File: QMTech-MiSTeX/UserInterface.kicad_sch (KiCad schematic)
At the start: 11 parts, among them SW1 XKB5858-W-F-75, SW2 TS-1187A-B-A-B, SW3 TS-1187A-B-A-B, SW4 TS-1187A-B-A-B, SW5 TS-1187A-B-A-B

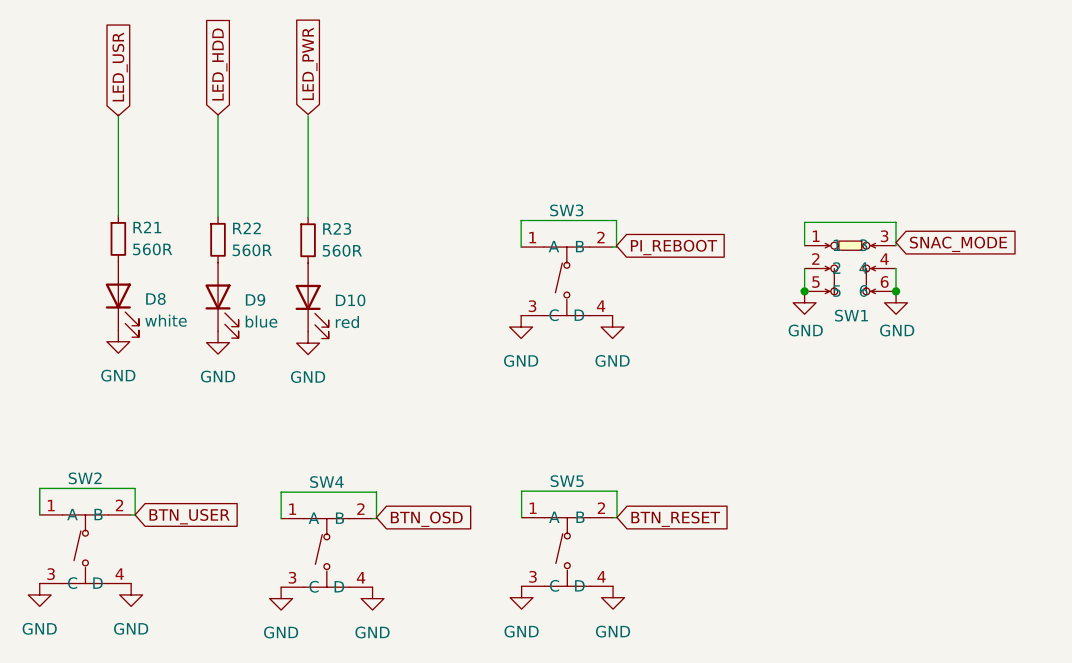
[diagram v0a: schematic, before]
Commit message: apply review notes from somhi, move audio into its own subsheet, add analog audio out
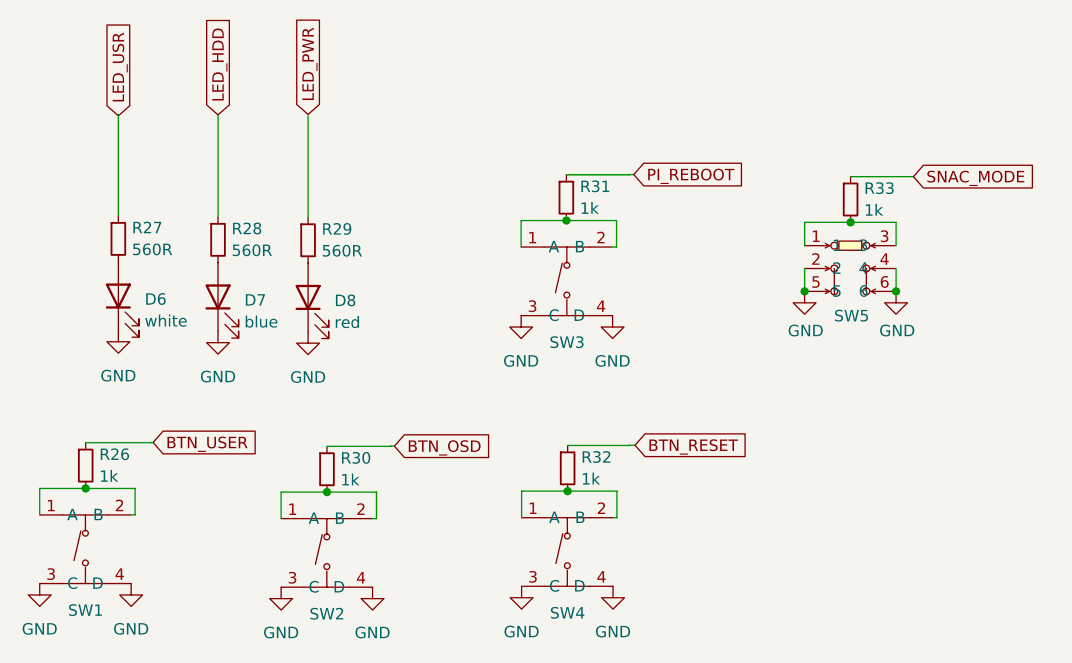
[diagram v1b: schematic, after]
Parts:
- added R26, R30, R31, R32, R33: 1k, R_0402_1005Metric, symbol jlcpcb-basic-resistor-0402:1k
- renumbered D8 to D6, D9 to D7, D10 to D8, R21 to R27, R22 to R28, R23 to R29, SW2 to SW1, SW4 to SW2, SW5 to SW4, SW1 to SW5
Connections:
- net BTN_OSD: now also R30.1; no longer SW2.1 (A), SW2.2 (B)
- net BTN_RESET: now also R32.1; no longer SW4.1 (A), SW4.2 (B)
- net BTN_USER: now also R26.1; no longer SW1.1 (A), SW1.2 (B)
- net PI_REBOOT: now also R31.1; no longer SW3.1 (A), SW3.2 (B)
- net SNAC_MODE: now also R33.1; no longer SW5.1, SW5.3
- new net: R32.2, SW4.1 (A), SW4.2 (B)
- new net: R33.2, SW5.1, SW5.3
- new net: R26.2, SW1.1 (A), SW1.2 (B)
- new net: R31.2, SW3.1 (A), SW3.2 (B)
- new net: R30.2, SW2.1 (A), SW2.2 (B)

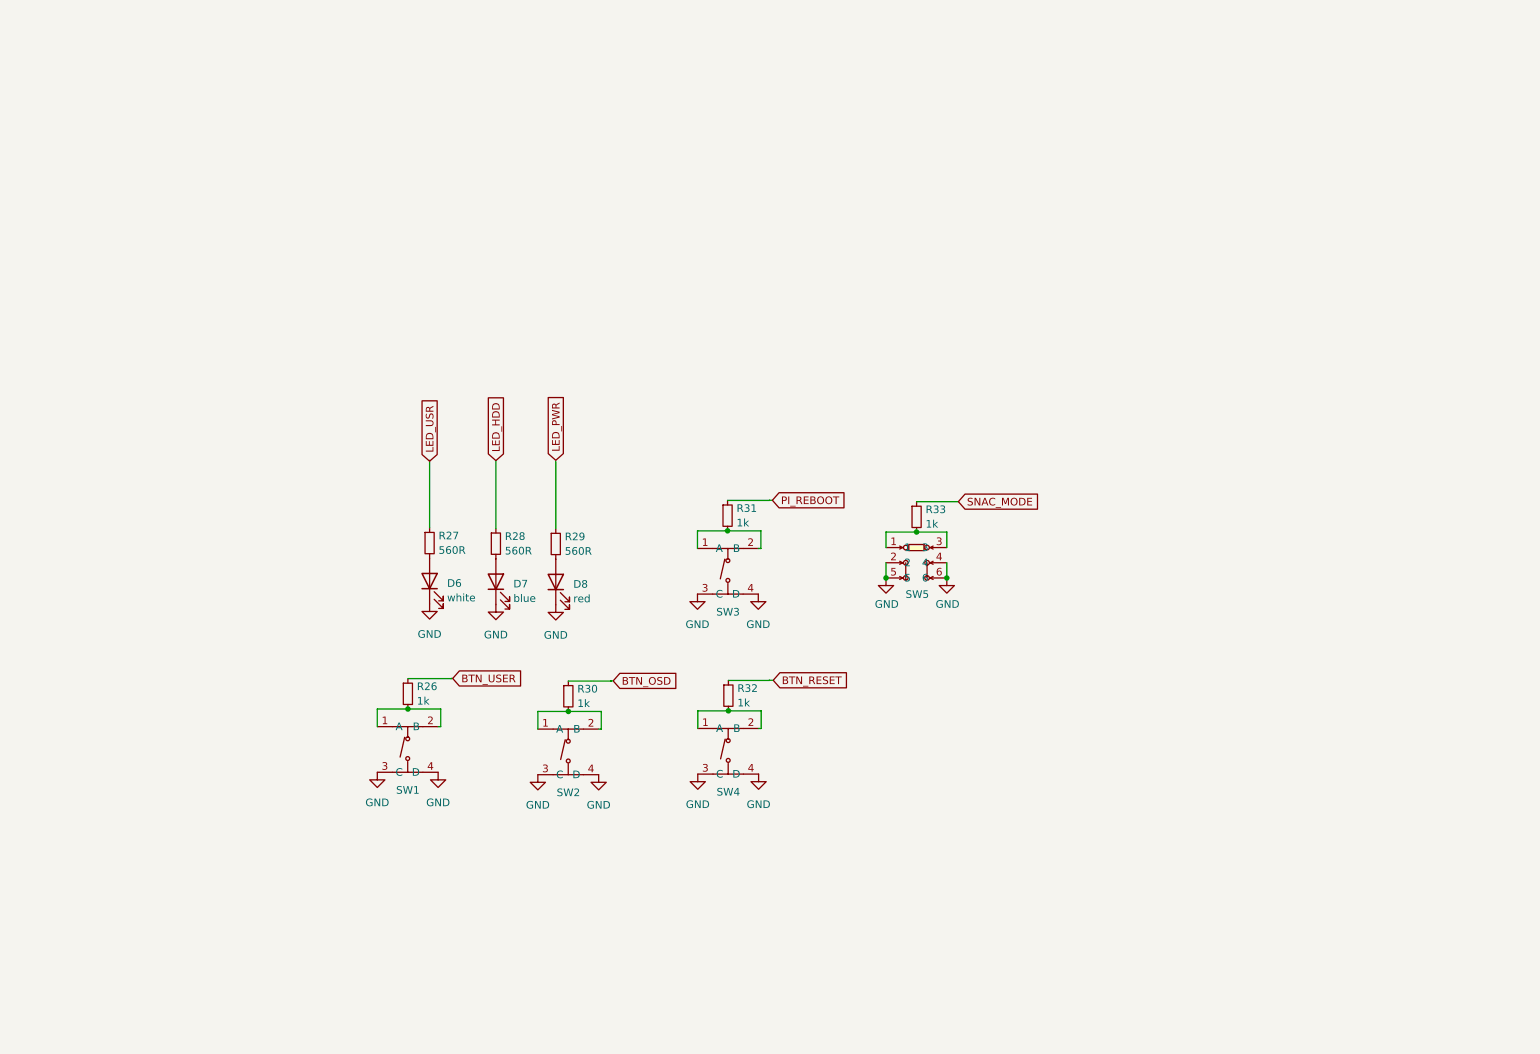
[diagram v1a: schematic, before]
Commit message: finish routing/layouting, fix silk screen, add mounting holes
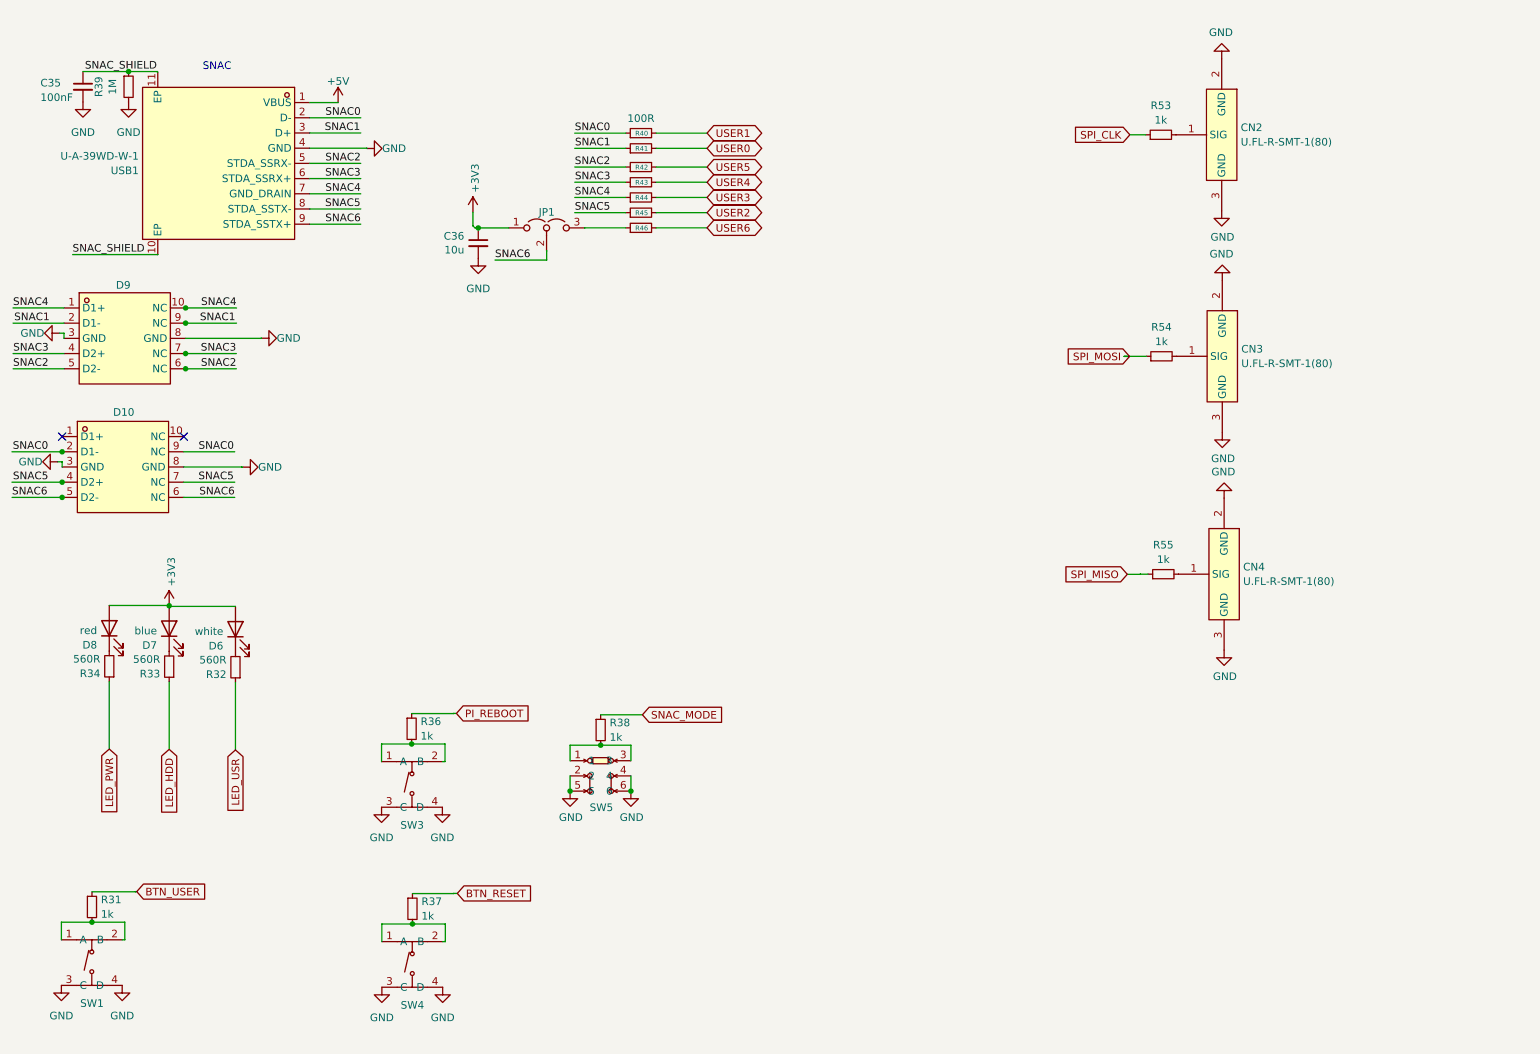
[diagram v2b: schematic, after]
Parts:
- removed R30: 1k, R_0402_1005Metric, symbol jlcpcb-basic-resistor-0402:1k
- removed SW2: TS-1187A-B-A-B, easyeda2kicad:SW-SMD_4P-L5.1-W5.1-P3.70-LS6.5-TL-2, symbol easyeda2kicad:TS-1187A-B-A-B
- added C35: 100nF, C_0402_1005Metric, symbol jlcpcb-basic-mlcc-0402:100nF
- added C36: 10u, Capacitor_SMD:C_0603_1608Metric, symbol Device:C_Small
- added CN2, CN3, CN4: U.FL-R-SMT-1(80), easyeda2kicad:RF-SMD_FRF05002-JSS103M, symbol easyeda2kicad:U.FL-R-SMT-1(80)
- added D10, D9: TPD4E05U06DQAR_C2972498, easyeda2kicad:DFN2510-10_L2.5-W1.0-P0.50-BL, symbol easyeda2kicad:TPD4E05U06DQAR_C2972498
- added JP1: Jumper_3_Open, Connector_PinHeader_2.54mm:PinHeader_1x03_P2.54mm_Vertical, symbol Jumper:Jumper_3_Open
- added R39: 1M, Resistor_SMD:R_0603_1608Metric, symbol Device:R_Small
- added R40, R41, R42, R43, R44, R45, R46: 100R, R_0402_1005Metric, symbol jlcpcb-basic-resistor-0402:100R
- added R53, R54, R55: 1k, R_0402_1005Metric, symbol jlcpcb-basic-resistor-0402:1k
- added USB1: U-A-39WD-W-1, easyeda2kicad:USB-A-SMD_U-A-39WD-W-1, symbol easyeda2kicad:U-A-39WD-W-1
- D6, D7, D8: footprint LED_0805_1608Metric -> LED_SMD:LED_0805_2012Metric
- renumbered R26 to R31, R27 to R32, R28 to R33, R29 to R34, R31 to R36, R32 to R37, R33 to R38
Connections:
- net GND: now also C35.2, C36.2, CN2.2 (GND), CN2.3 (GND), CN3.2 (GND), CN3.3 (GND), CN4.2 (GND), CN4.3 (GND), D10.3 (GND), D10.8 (GND), D9.3 (GND), D9.8 (GND), R39.2, USB1.4 (GND); no longer D6.1 (K), D7.1 (K), D8.1 (K)
- net LED_HDD: now also R33.1
- net LED_PWR: now also R34.1
- net at R34.2: now also D8.1 (K); no longer D8.2 (A)
- net at R33.2: now also D7.1 (K); no longer D7.2 (A)
- net at R32.2: now also D6.1 (K); no longer D6.2 (A)
- new net: CN4.1 (SIG), R55.2
- new net: CN2.1 (SIG), R53.2
- new net: JP1.3 (B), R46.1
- new net: CN3.1 (SIG), R54.2
- new net +3V3: C36.1, D6.2 (A), D7.2 (A), D8.2 (A), JP1.1 (A)
- new net +5V: USB1.1 (VBUS)
- new net SNAC0: D10.2 (D1-), D10.9 (NC), R40.1, USB1.2 (D-)
- new net SNAC1: D9.2 (D1-), D9.9 (NC), R41.1, USB1.3 (D+)
- new net SNAC2: D9.5 (D2-), D9.6 (NC), R42.1, USB1.5 (STDA_SSRX-)
- new net SNAC3: D9.4 (D2+), D9.7 (NC), R43.1, USB1.6 (STDA_SSRX+)
- new net SNAC4: D9.1 (D1+), D9.10 (NC), R44.1, USB1.7 (GND_DRAIN)
- new net SNAC5: D10.4 (D2+), D10.7 (NC), R45.1, USB1.8 (STDA_SSTX-)
- new net SNAC6: D10.5 (D2-), D10.6 (NC), JP1.2 (C), USB1.9 (STDA_SSTX+)
- new net SNAC_SHIELD: C35.1, R39.1, USB1.10 (EP), USB1.11 (EP)
- new net SPI_CLK: R53.1
- new net SPI_MISO: R55.1
- new net SPI_MOSI: R54.1
- new net USER0: R41.2
- new net USER1: R40.2
- new net USER2: R45.2
- new net USER3: R44.2
- new net USER4: R43.2
- new net USER5: R42.2
- new net USER6: R46.2
- no-connect marks 0 -> 2
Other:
- note added: "SNAC"
- moved on the sheet: D6, D7, D8, R31, R32, R33, R34, R36, R37, R38, SW1, SW3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

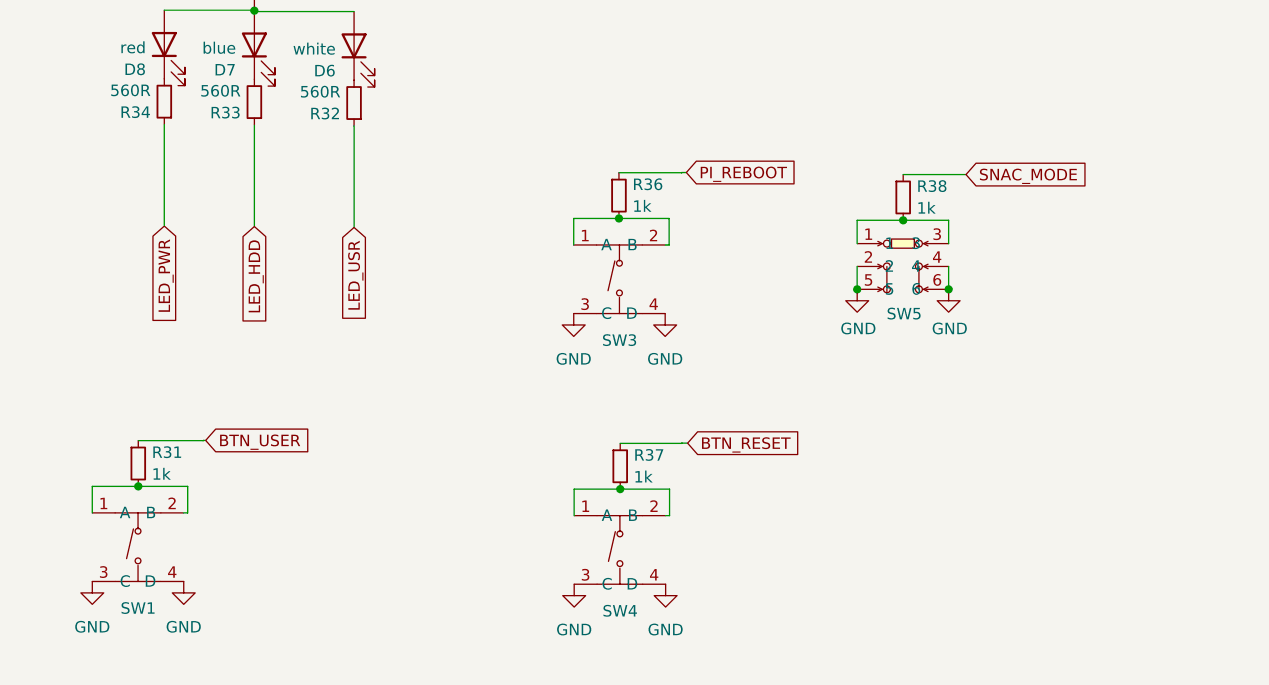
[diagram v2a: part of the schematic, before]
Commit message: get rid of SNAC mode switch and add OSD button instead
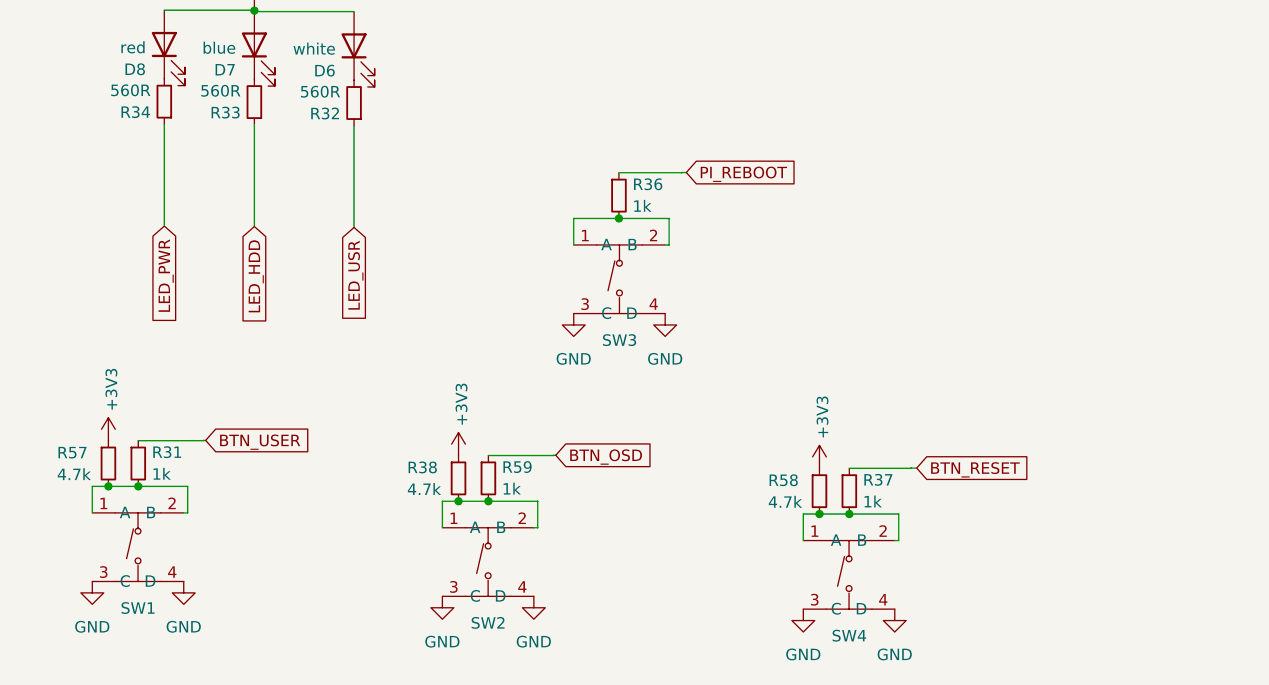
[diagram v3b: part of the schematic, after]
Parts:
- removed R38: 1k, R_0402_1005Metric, symbol jlcpcb-basic-resistor-0402:1k
- removed SW5: XKB5858-W-F-75, easyeda2kicad:SW-SMD_XKB5858-W-F-75, symbol easyeda2kicad:XKB5858-W-F-75
- added R38, R57, R58: 4.7k, R_0402_1005Metric, symbol jlcpcb-basic-resistor:R_0402_4.7k
- added R59: 1k, R_0402_1005Metric, symbol jlcpcb-basic-resistor-0402:1k
- added SW2: TS-1187A-B-A-B, easyeda2kicad:SW-SMD_4P-L5.1-W5.1-P3.70-LS6.5-TL-2, symbol easyeda2kicad:TS-1187A-B-A-B
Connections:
- net +3V3: now also R38.1, R57.1, R58.1
- net GND: now also SW2.3 (C), SW2.4 (D)
- net at R37.2, SW4.1 (A), SW4.2 (B): now also R58.2
- net at R31.2, SW1.1 (A), SW1.2 (B): now also R57.2
- new net: R38.2, R59.2, SW2.1 (A), SW2.2 (B)
- new net BTN_OSD: R59.1
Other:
- moved on the sheet: R37, SW4

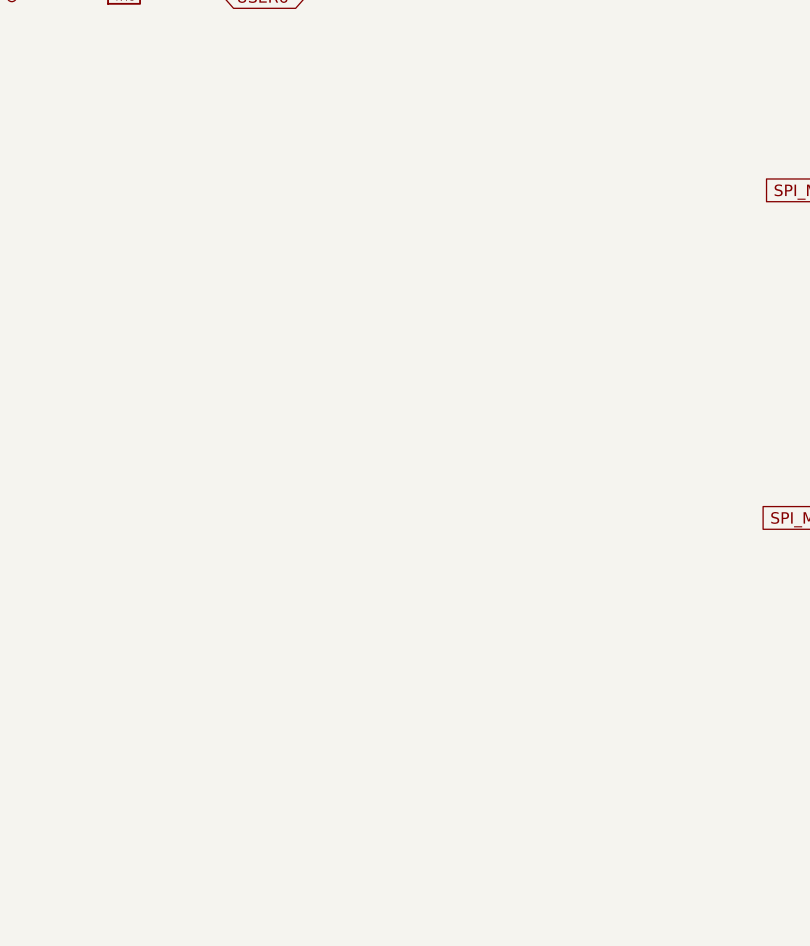
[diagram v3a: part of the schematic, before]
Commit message: QMTech-MiSTeX: OSHW logo on front mask, add instructions for installing SDRAM
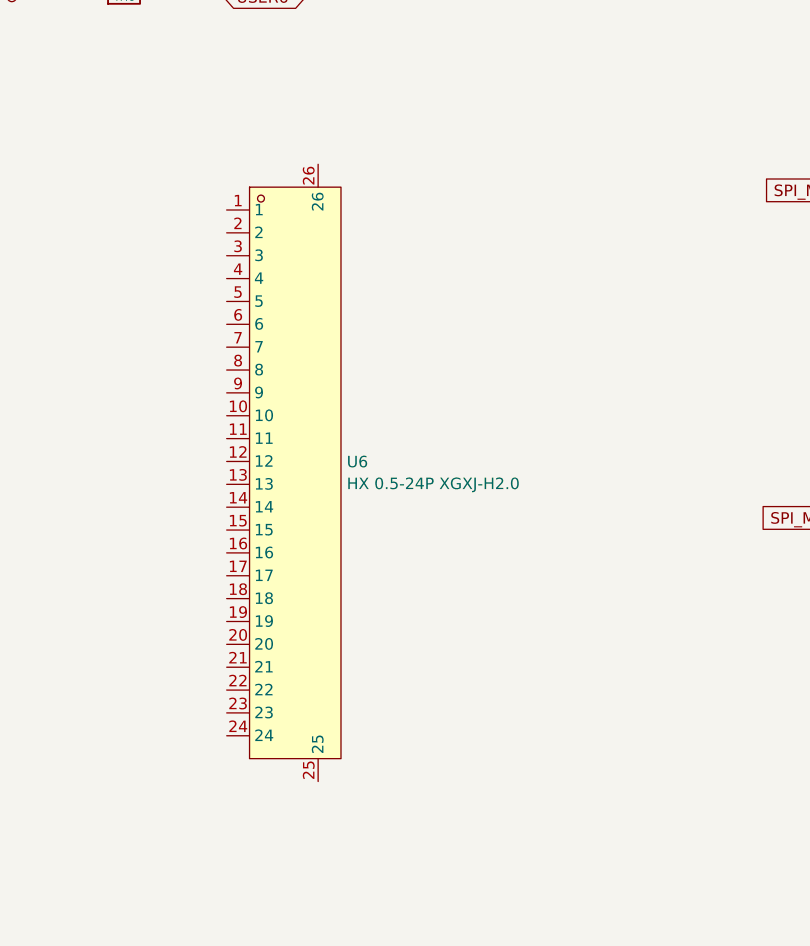
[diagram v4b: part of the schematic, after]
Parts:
- added U6: HX 0.5-24P XGXJ-H2.0, easyeda2kicad:CONN-SMD_24P-P0.50_HANXIA_HX0.5-24PXGXJ-H2.0, symbol easyeda2kicad:HX0.5-24PXGXJ-H2.0
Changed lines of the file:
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@@
+    )
+  )
+  (symbol (lib_id "easyeda2kicad:HX0.5-24PXGXJ-H2.0") (at 148.2598 107.5182 0) (unit 1)
+    (in_bom yes) (on_board yes) (dnp no) (fields_autoplaced)
+    (property "Reference" "U6" (at 156.5148 105.0361 0)
+      (effects (font (size 1.27 1.27)) (justify left))
+    )
+    (property "Value" "HX 0.5-24P XGXJ-H2.0" (at 156.5148 107.4603 0)
+      (effects (font (size 1.27 1.27)) (justify left))
+    )
+    (property "Footprint" "easyeda2kicad:CONN-SMD_24P-P0.50_HANXIA_HX0.5-24PXGXJ-H2.0" (at 148.2598 148.1582 0)
+      (effects (font (size 1.27 1.27)) hide)
+    )
+    (property "Datasheet" "" (at 148.2598 107.5182 0)
+      (effects (font (size 1.27 1.27)) hide)
+    )
+    (property "LCSC Part" "C5142050" (at 148.2598 150.6982 0)
+      (effects (font (size 1.27 1.27)) hide)
+    )
+    (pin "3")
+    (pin "26")
+    (pin "24")
+    (pin "8")
+    (pin "4")
+    (pin "7")
+    (pin "15")
+    (pin "14")
+    (pin "12")
+    (pin "13")
+    (pin "11")
+    (pin "6")
+    (pin "19")
+    (pin "9")
+    (pin "1")
+    (pin "10")
+    (pin "2")
+    (pin "22")
+    (pin "16")
+    (pin "21")
+    (pin "18")
+    (pin "20")
+    (pin "5")
+    (pin "23")
+    (pin "17")
+    (pin "25")
+    (instances
+      (project "QMTech-MiSTeX"
+        (path "/bf95850e-2fcb-4784-a603-f17fc357556b/cce2b405-ae09-44af-ba42-d113d6ffe521"
+          (reference "U6") (unit 1)
+        )
+      )
     )
   )
